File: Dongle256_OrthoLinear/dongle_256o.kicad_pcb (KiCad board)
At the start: 2 copper layers, 138.1 x 98.1 mm, 61 parts, among them SW1 GateronLP, SW10 GateronLP, SW11 GateronLP, SW12 GateronLP, SW13 GateronLP, SW14 GateronLP, SW15 GateronLP, SW16 GateronLP, SW17 GateronLP, SW18 GateronLP, SW19 GateronLP, SW2 GateronLP, SW20 GateronLP, SW21 GateronLP, SW22 GateronLP, SW23 GateronLP, SW24 GateronLP, SW25 GateronLP, SW26 GateronLP, SW27 GateronLP, SW28 GateronLP, SW29 GateronLP, SW3 GateronLP, SW30 GateronLP, SW4 GateronLP, SW5 GateronLP, SW6 GateronLP, SW7 GateronLP, SW8 GateronLP, SW9 GateronLP, U1 NRF52840-DONGLE

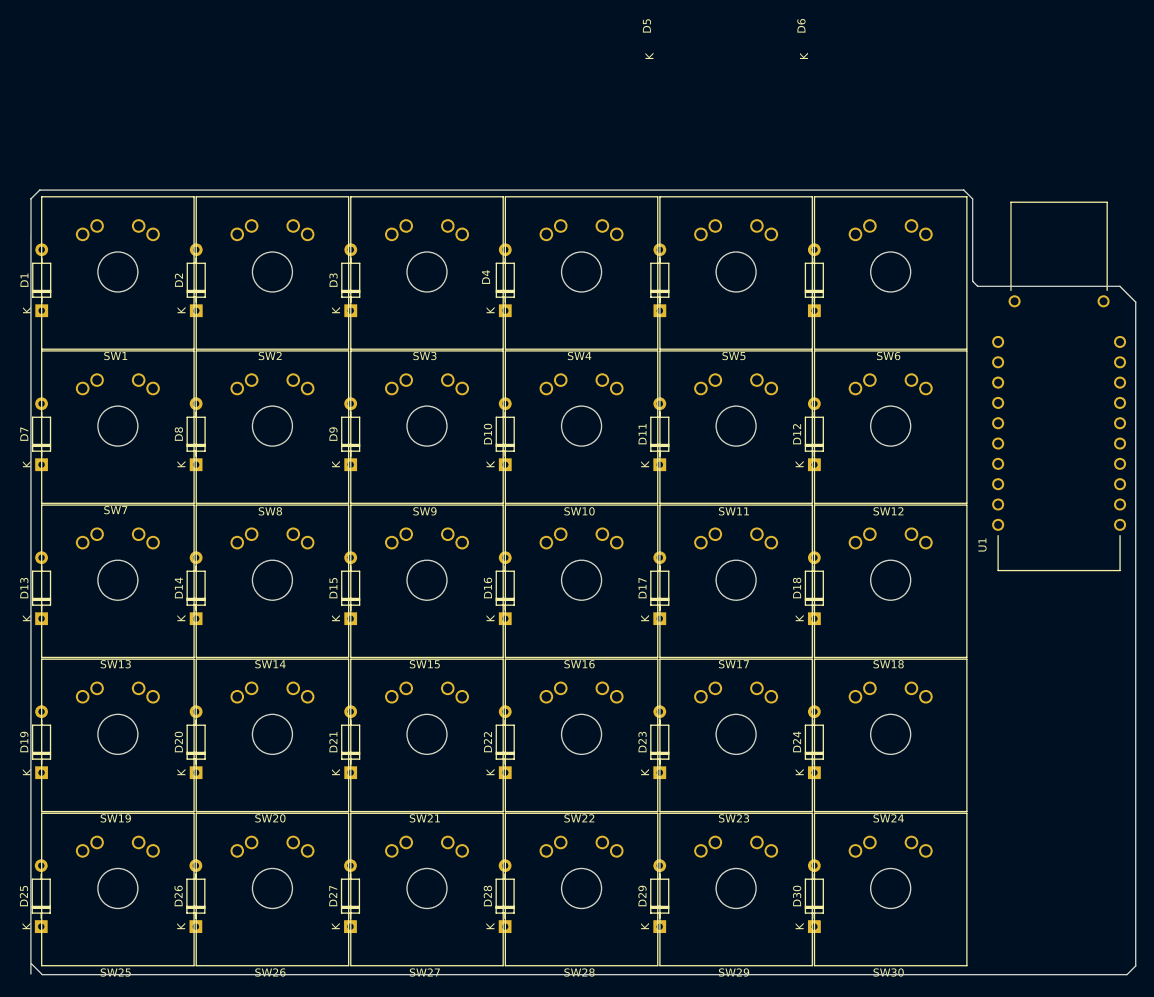
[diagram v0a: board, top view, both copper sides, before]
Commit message: PCB design without switch
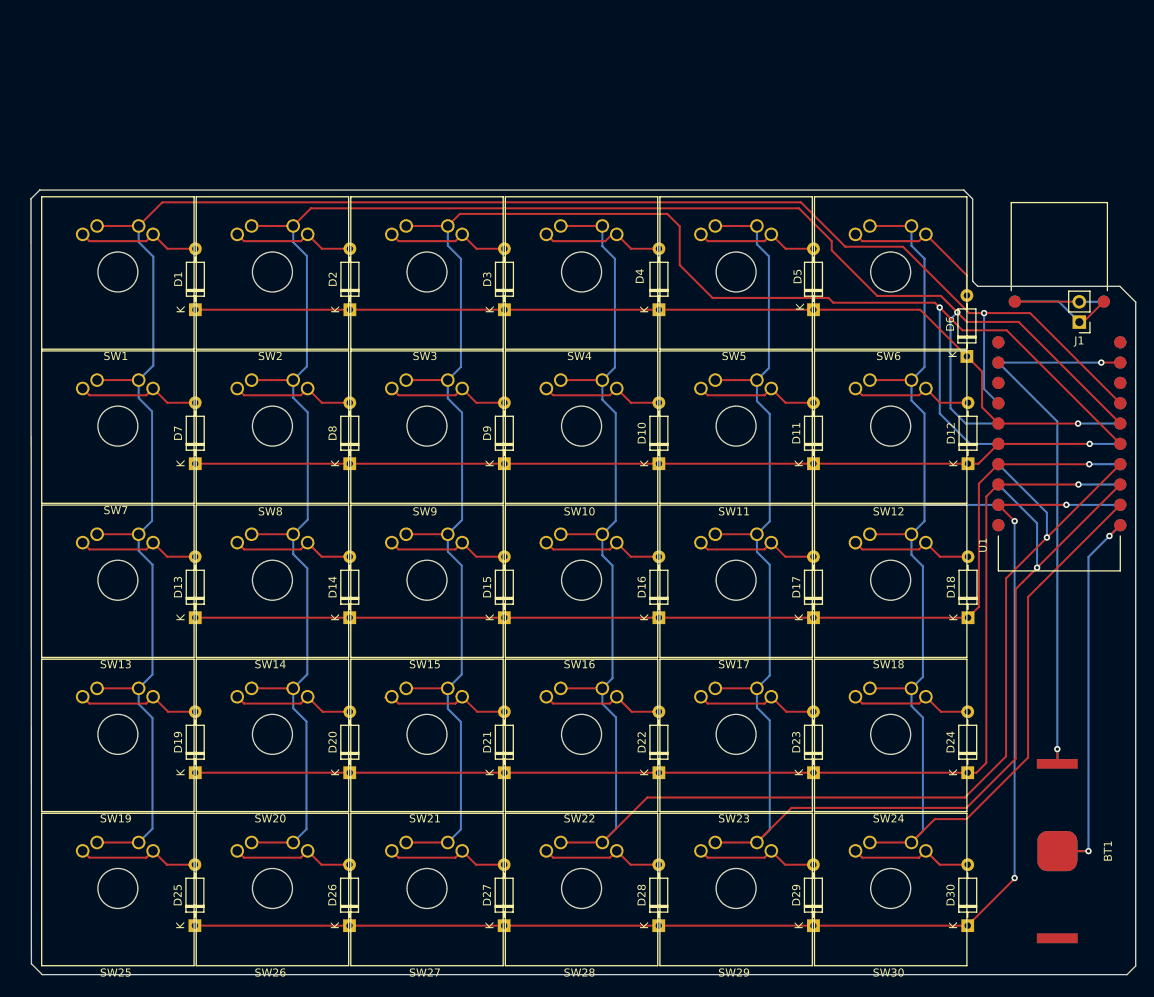
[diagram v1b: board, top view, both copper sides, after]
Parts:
- added BT1: Battery_Cell, MVB:TBH-CR2032-M04, F.Cu at (156.2, 123.5)
- added BT2: Battery_Cell, MVB:TBH-CR2032-M04, B.Cu at (156.2, 123.5)
- added J1: Conn_01x02_Male, Connector_PinHeader_2.54mm:PinHeader_1x02_P2.54mm_Vertical, F.Cu at (158.9, 57.4)
- added U2: NRF52840-DONGLE, download:MODULE_NRF52840-DONGLE, B.Cu at (156.4, 65.5)
- moved D6 19.9 mm to (144.9, 61.7)
- moved D12 19.2 mm to (145.0, 75.1)
- moved D18 19.2 mm to (145.0, 94.4)
- moved D4 19.2 mm to (106.4, 55.9)
- moved D13 19.2 mm to (48.4, 94.4)
- moved D25 19.2 mm to (48.4, 132.9)
- moved D7 19.2 mm to (48.4, 75.1)
- moved D1 19.2 mm to (48.5, 55.9)
- moved D10 19.2 mm to (106.4, 75.1)
- moved D11 19.2 mm to (125.7, 75.1)
- moved D14 19.2 mm to (67.8, 94.4)
- moved D15 19.2 mm to (87.1, 94.4)
- moved D16 19.2 mm to (106.4, 94.4)
- moved D17 19.2 mm to (125.7, 94.4)
- moved D2 19.2 mm to (67.8, 55.9)
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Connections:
- U1 pad 0.09: Net-(D10-Pad1) -> Net-(D19-Pad1)
- U1 pad 0.10: Net-(D1-Pad1) -> Net-(D25-Pad1)
- U1 pad 0.13: unconnected-(U1-Pad0.13) -> Net-(U1-Pad0.13)
- U1 pad 0.15: unconnected-(U1-Pad0.15) -> Net-(U1-Pad0.15)
- U1 pad 0.17: unconnected-(U1-Pad0.17) -> Net-(U1-Pad0.17)
- U1 pad 0.20: unconnected-(U1-Pad0.20) -> Net-(U1-Pad0.20)
- U1 pad 0.22: Net-(D25-Pad1) -> Net-(D1-Pad1)
- U1 pad 0.24: Net-(D19-Pad1) -> Net-(D10-Pad1)
- U1 pad OUT: unconnected-(U1-PadOUT) -> Net-(BT1-Pad1)
- U1 pad SWDCLK: unconnected-(U1-PadSWDCLK) -> Net-(J1-Pad1)
- U1 pad SWDIO: unconnected-(U1-PadSWDIO) -> Net-(J1-Pad2)
- U1 pad VBUS: unconnected-(U1-PadVBUS) -> Net-(U1-PadVBUS)
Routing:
- net Net-(SW1-Pad1): track 0.00 -> 255.2 mm, vias 0 -> 1
- net Net-(SW14-Pad1): track 0.00 -> 244.2 mm, vias 0 -> 1
- net Net-(SW15-Pad1): track 0.00 -> 230.3 mm, vias 0 -> 1
- net Net-(SW10-Pad1): track 0.00 -> 217.3 mm, vias 0 -> 1
- net Net-(SW11-Pad1): track 0.00 -> 197.1 mm, vias 0 -> 1
- net Net-(SW12-Pad1): track 0.00 -> 172.7 mm
- net Net-(D25-Pad1): track 0.00 -> 167.7 mm, vias 0 -> 3
- net Net-(D19-Pad1): track 0.00 -> 150.1 mm, vias 0 -> 1
- net Net-(D13-Pad1): track 0.00 -> 132.6 mm, vias 0 -> 1
- net Net-(D1-Pad1): track 0.00 -> 124.1 mm, vias 0 -> 1
- net Net-(D10-Pad1): track 0.00 -> 116.7 mm, vias 0 -> 1
- net Net-(BT1-Pad1): track 0.00 -> 70.3 mm, vias 0 -> 2
- net Net-(BT1-Pad2): track 0.00 -> 52.1 mm, vias 0 -> 2
- net Net-(D6-Pad2): track 0.00 -> 19.3 mm
- net Net-(D21-Pad2): track 0.00 -> 16.4 mm
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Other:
- outline, holes or cut-outs redrawn

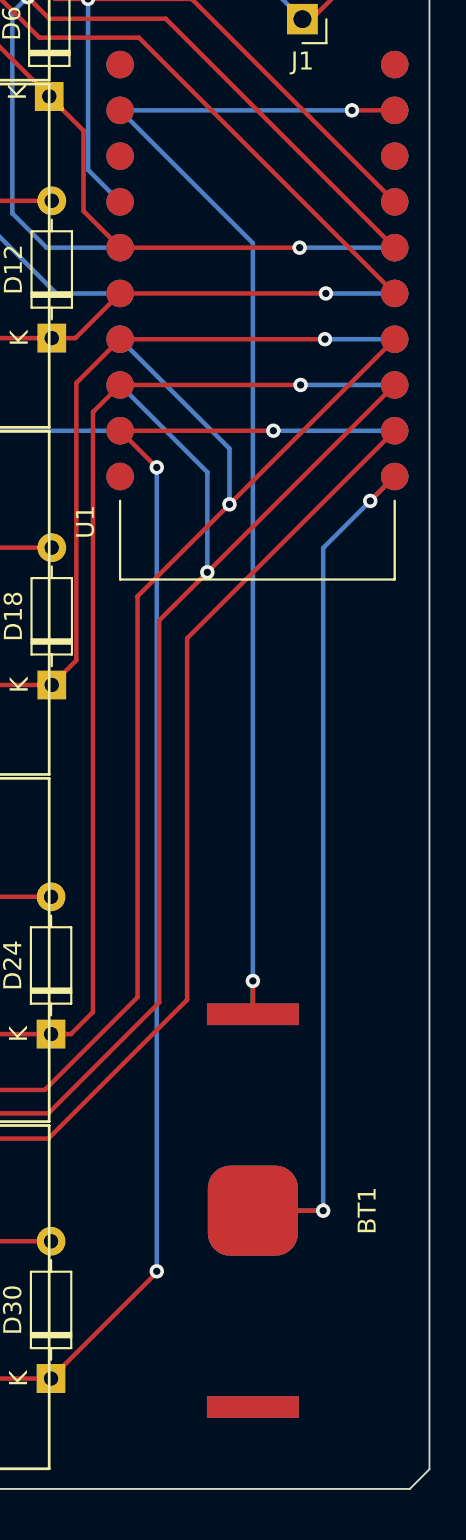
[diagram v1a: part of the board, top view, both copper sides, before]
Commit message: Update on off and slider switch
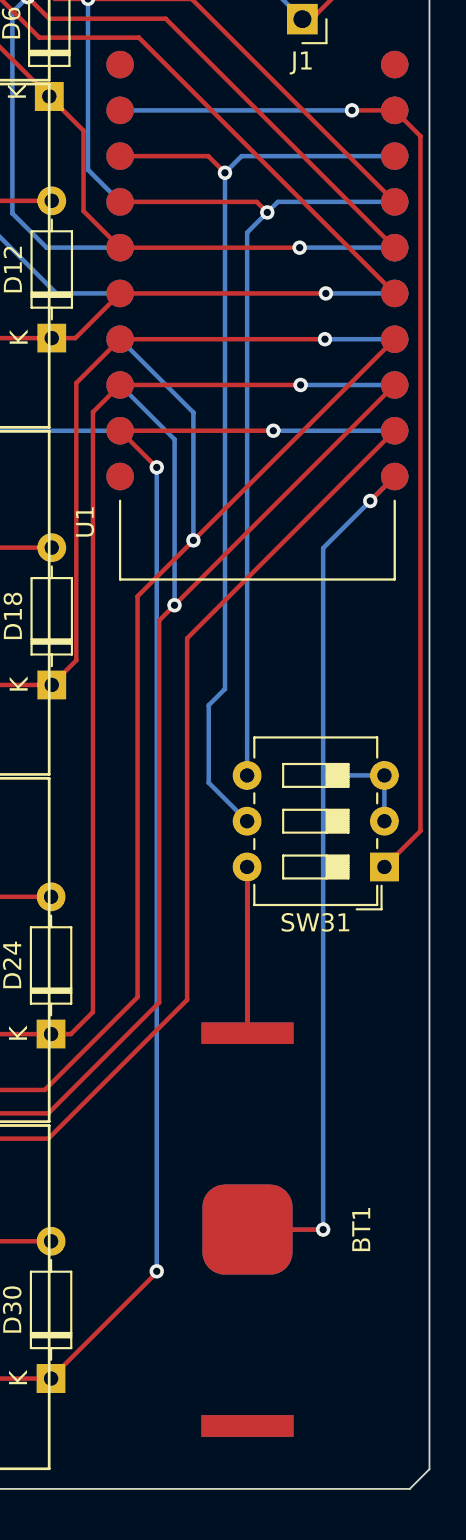
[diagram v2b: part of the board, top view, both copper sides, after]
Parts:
- added SW31: SW_DIP_x03, Button_Switch_THT:SW_DIP_SPSTx03_Slide_6.7x9.18mm_W7.62mm_P2.54mm_LowProfile, F.Cu at (163.5, 104.5)
- moved BT1 1.09 mm to (155.9, 124.6)
- moved BT2 1.09 mm to (155.9, 124.6)
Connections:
- U1 pad OUT: Net-(BT1-Pad1) -> Net-(SW31-Pad1)
- U2 pad OUT: Net-(BT1-Pad1) -> Net-(SW31-Pad1)
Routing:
- net Net-(SW31-Pad1): track 0.00 -> 58.7 mm, vias 0 -> 1
- net Net-(SW31-Pad5): track 0.00 -> 53.2 mm, vias 0 -> 1
- net Net-(BT1-Pad1): track 70.3 -> 18.5 mm, vias 2 -> 0
- net Net-(SW31-Pad4): track 0.00 -> 47.4 mm, vias 0 -> 1
- net Net-(BT1-Pad2): track 52.1 -> 59.7 mm
- net Net-(SW10-Pad1): track 217.3 -> 218.4 mm
- net Net-(SW11-Pad1): track 197.1 -> 198.1 mm

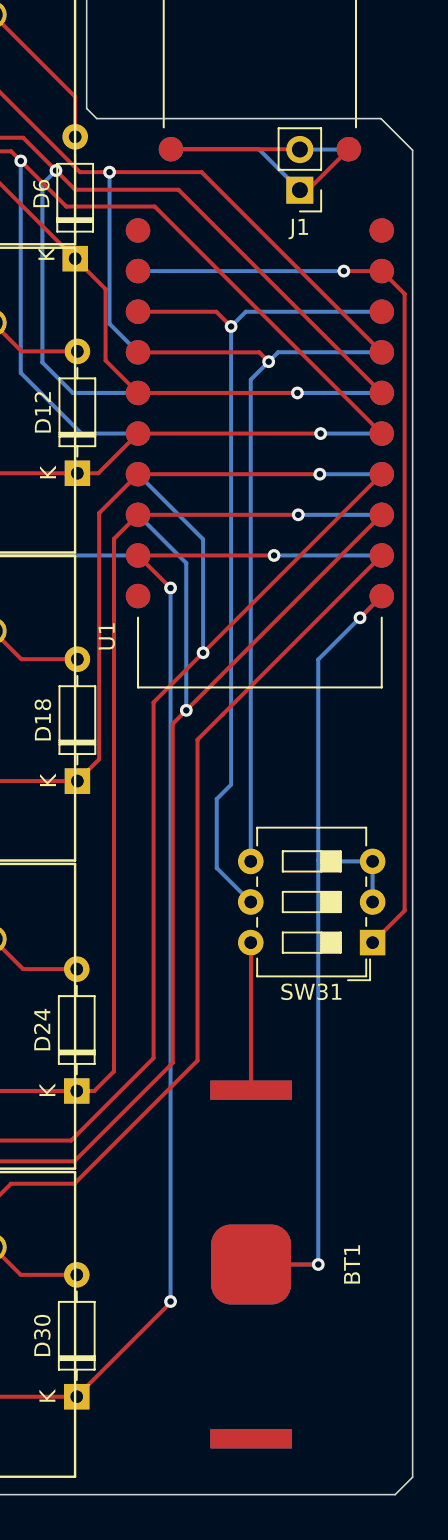
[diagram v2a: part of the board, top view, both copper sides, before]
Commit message: Update flashing pads and redo the status switch.
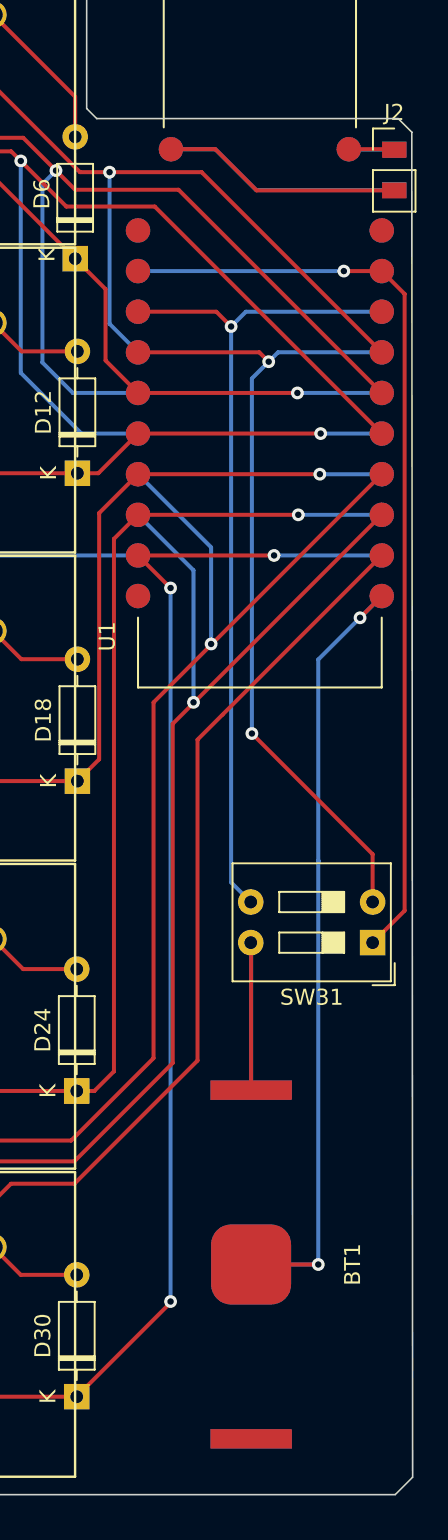
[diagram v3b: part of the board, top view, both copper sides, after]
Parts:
- added J2: Conn_01x02_Male, Connector_PinHeader_2.54mm:PinHeader_1x02_P2.54mm_Vertical, F.Cu at (164.8, 54.9)
- J1: moved to B.Cu
- SW31: footprint Button_Switch_THT:SW_DIP_SPSTx03_Slide_6.7x9.18mm_W7.62mm_P2.54mm_LowProfile -> Button_Switch_THT:SW_DIP_SPSTx02_Slide_9.78x7.26mm_W7.62mm_P2.54mm
- moved J1 5.90 mm to (164.8, 57.4), turned to 0 degrees
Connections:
- SW31 pad 2: Net-(BT1-Pad2) -> Net-(SW31-Pad2)
- SW31 pad 3: Net-(BT1-Pad2) -> Net-(SW31-Pad3)
- SW31 pad 4: Net-(SW31-Pad4) -> Net-(BT1-Pad1)
- U1 pad 0.17: Net-(SW31-Pad5) -> Net-(SW31-Pad3)
- U1 pad 0.20: Net-(SW31-Pad4) -> Net-(SW31-Pad2)
- U2 pad 0.17: Net-(SW31-Pad5) -> Net-(SW31-Pad3)
- U2 pad 0.20: Net-(SW31-Pad4) -> Net-(SW31-Pad2)
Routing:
- net Net-(SW31-Pad5): track 53.2 -> 0.00 mm, vias 1 -> 0
- net Net-(SW31-Pad2): track 0.00 -> 53.1 mm, vias 0 -> 2
- net Net-(SW31-Pad3): track 0.00 -> 52.5 mm, vias 0 -> 1
- net Net-(SW31-Pad4): track 47.4 -> 0.00 mm, vias 1 -> 0
- net Net-(J1-Pad2): track 11.1 -> 17.9 mm
- net Net-(BT1-Pad2): track 59.7 -> 53.8 mm
- net Net-(J1-Pad1): track 13.2 -> 17.9 mm
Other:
- outline, holes or cut-outs redrawn
